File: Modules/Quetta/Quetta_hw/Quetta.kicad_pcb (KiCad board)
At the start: 2 copper layers, 89 parts, among them Q1 IRLML9303, SW1 SWITCH_H

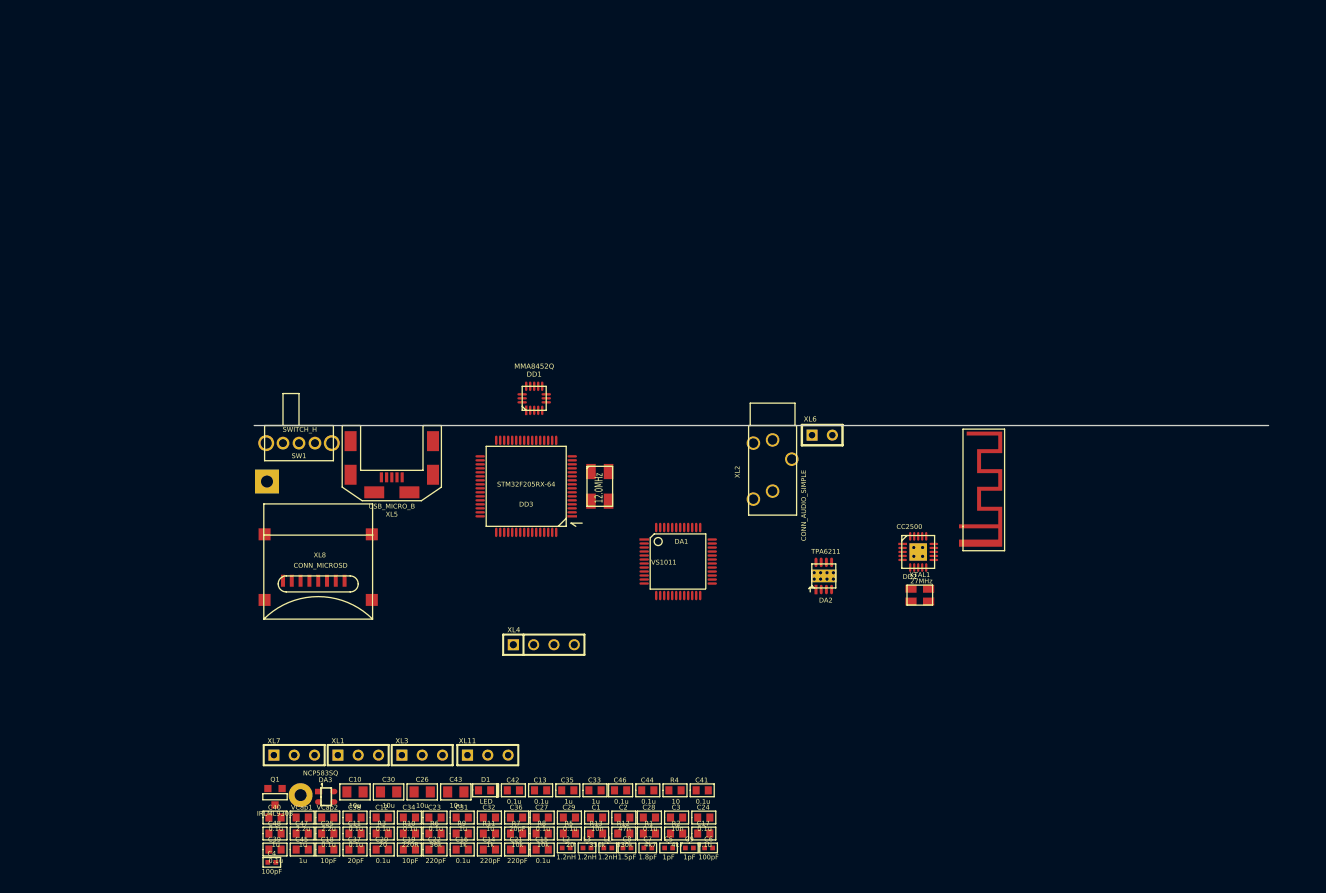
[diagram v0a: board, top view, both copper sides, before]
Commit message: 
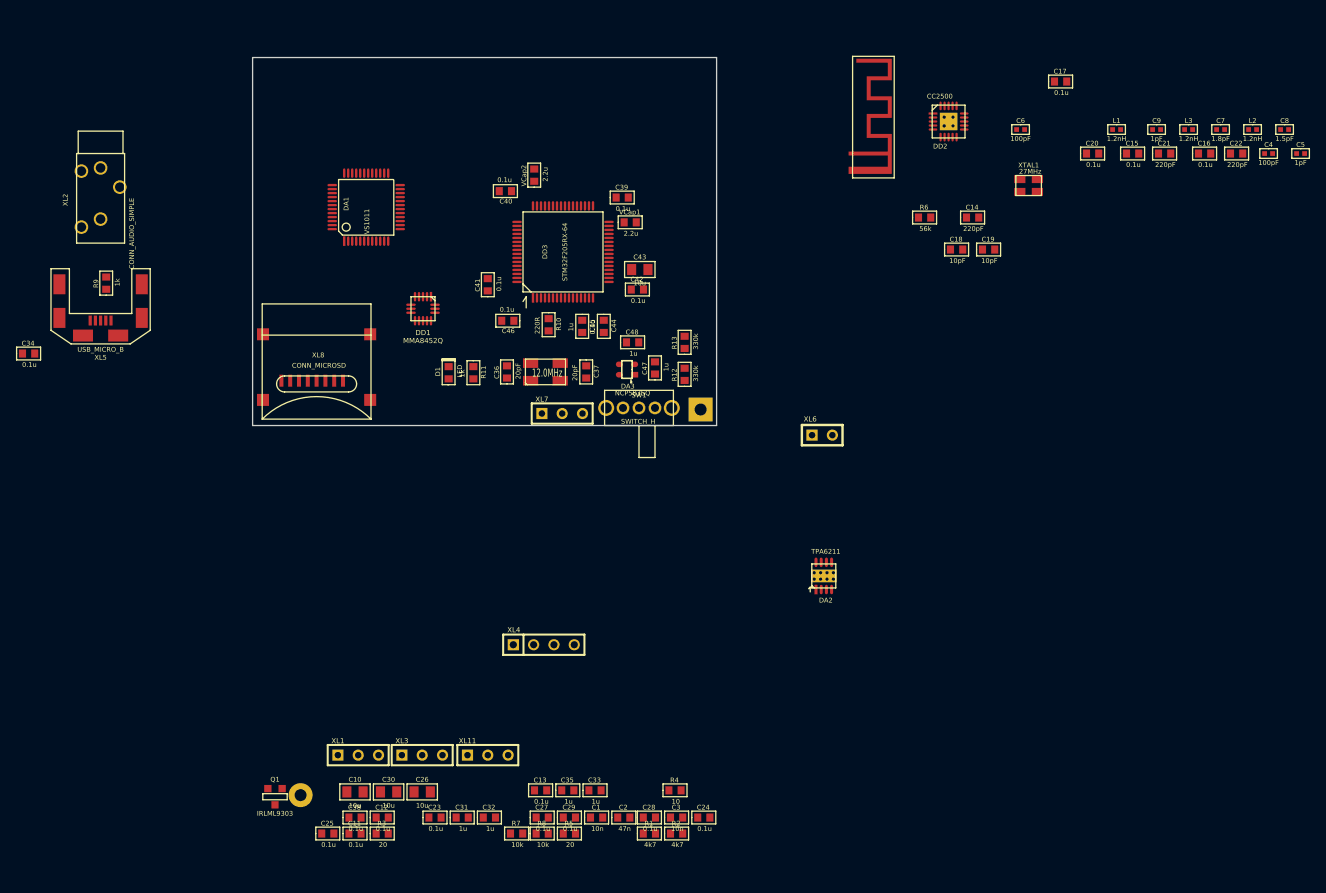
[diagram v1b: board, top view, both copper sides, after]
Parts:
- moved C4 152.9 mm to (287.0, 106.0)
- moved C22 132.7 mm to (283.0, 106.0)
- moved C16 127.2 mm to (279.0, 106.0)
- moved C20 124.3 mm to (265.0, 106.0)
- moved L2 124.2 mm to (285.0, 103.0)
- moved C8 121.7 mm to (289.0, 103.0)
- moved C21 118.9 mm to (274.0, 106.0)
- moved C5 117.4 mm to (291.0, 106.0)
- moved L3 117.1 mm to (277.0, 103.0)
- moved C7 114.9 mm to (281.0, 103.0)
- moved C15 114.1 mm to (270.0, 106.0)
- moved L1 110.0 mm to (268.0, 103.0)
- moved C18 108.6 mm to (248.0, 118.0)
- moved C9 107.1 mm to (273.0, 103.0)
- moved C19 104.2 mm to (252.0, 118.0)
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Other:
- board outline added: 58 x 46 mm

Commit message: 
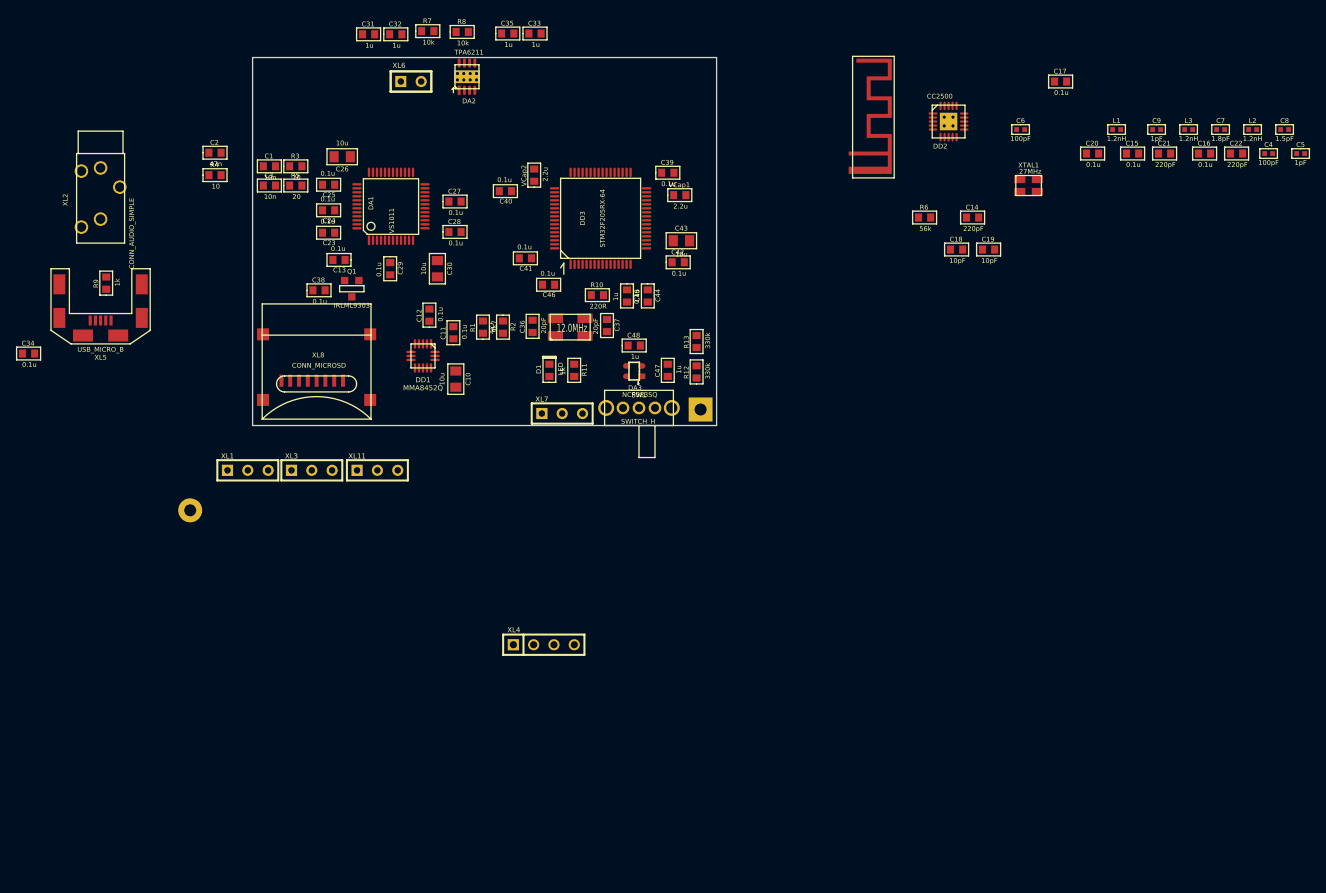
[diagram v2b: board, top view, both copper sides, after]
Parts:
- moved R7 100.9 mm to (181.9, 90.7)
- moved R8 100.7 mm to (186.2, 90.8)
- moved C31 98.6 mm to (174.5, 91.1)
- moved C32 98.6 mm to (177.9, 91.1)
- moved C2 97.6 mm to (155.3, 105.9)
- moved R4 96.0 mm to (155.3, 108.7)
- moved C33 94.9 mm to (195.3, 91.0)
- moved C35 94.9 mm to (191.9, 91.0)
- moved C3 94.0 mm to (162.1, 110.0)
- moved C1 91.1 mm to (162.1, 107.6)
- moved C24 89.2 mm to (169.5, 113.1), turned to 180 degrees
- moved R5 87.9 mm to (165.4, 110.0)
- moved R3 84.1 mm to (165.4, 107.6)
- moved C25 81.1 mm to (169.5, 109.9), turned to 180 degrees
- moved C26 80.0 mm to (171.2, 106.4), turned to 180 degrees
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
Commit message: quetta fsx added
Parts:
- moved XL10 78.5 mm to (216.0, 104.9)
- moved C8 71.0 mm to (223.9, 131.6), turned to 180 degrees
- moved C5 70.9 mm to (223.3, 127.2), turned to 270 degrees
- moved L2 66.2 mm to (224.4, 129.7), turned to 90 degrees
- moved C4 65.5 mm to (223.8, 123.0), turned to 270 degrees
- moved C7 63.9 mm to (222.7, 129.2), turned to 180 degrees
- moved XL4 63.1 mm to (192.9, 104.4)
- moved XL1 59.3 mm to (202.0, 104.4)
- moved L3 57.1 mm to (225.3, 127.2), turned to 90 degrees
- moved XL11 53.6 mm to (209.9, 104.4)
- moved C9 52.2 mm to (225.8, 125.3)
- moved L1 50.4 mm to (222.8, 125.3)
- moved C16 49.5 mm to (229.6, 106.5), turned to 90 degrees
- moved C21 49.1 mm to (225.2, 112.2), turned to 270 degrees
- moved C22 47.9 mm to (235.2, 109.5)
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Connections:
- ANT1 pad 1: N-0000038 -> GND
- C8 pad 1: N-0000038 -> GND
- L2 pad 1: N-0000038 -> GND
- SW1 pad 1: /BATTERY_PLUS -> (no net)
- SW1 pad 3: (no net) -> /BATTERY_PLUS
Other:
- net class Default: clearance 0.254 -> 0.2; trace_width 0.254 -> 0.2; via_dia 0.889 -> 0.9; via_drill 0.635 -> 0.4
- net class wide added: clearance 0.2, trace_width 0.5, via_dia 0.9, via_drill 0.4
- rule trace_clearance: 0.254 -> 0.2
- rule trace_min: 0.254 -> 0.2
- rule via_min_drill: 0.508 -> 0.4
- rule via_min_size: 0.889 -> 0.9

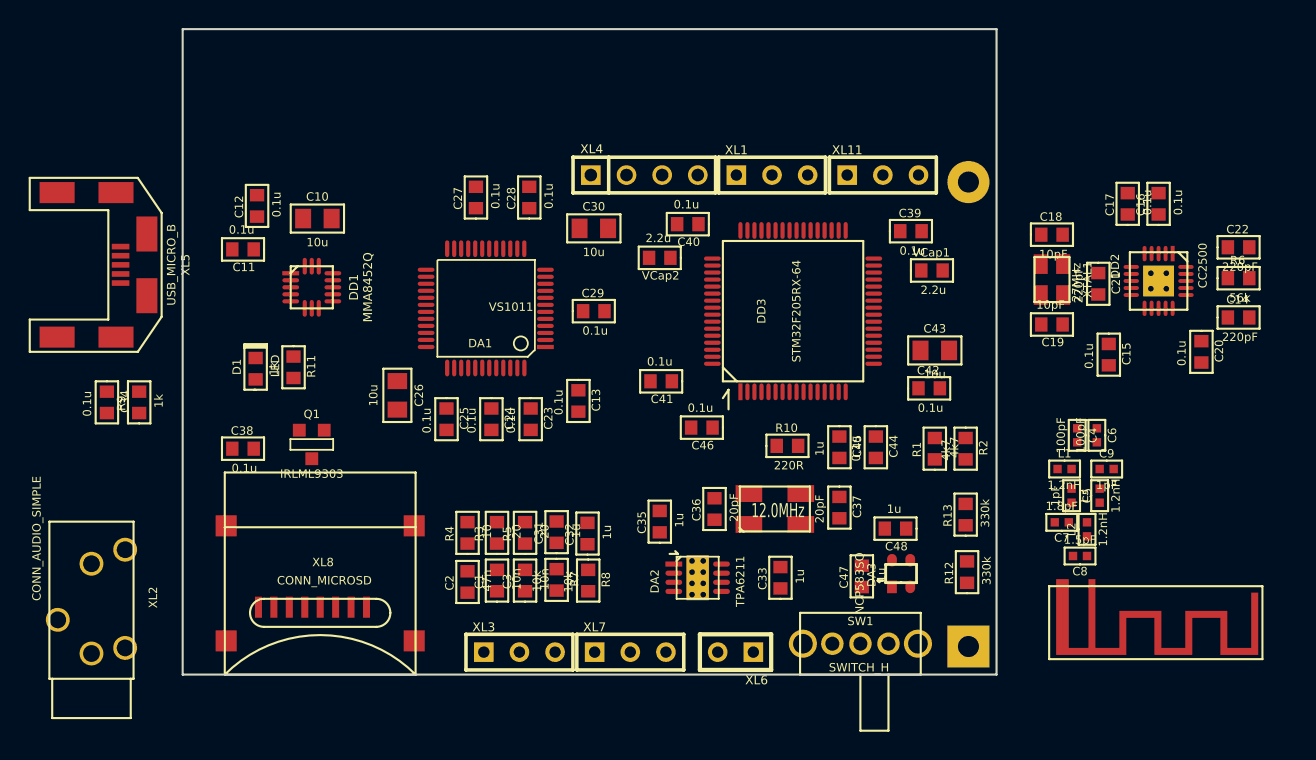
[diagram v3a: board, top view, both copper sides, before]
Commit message: 
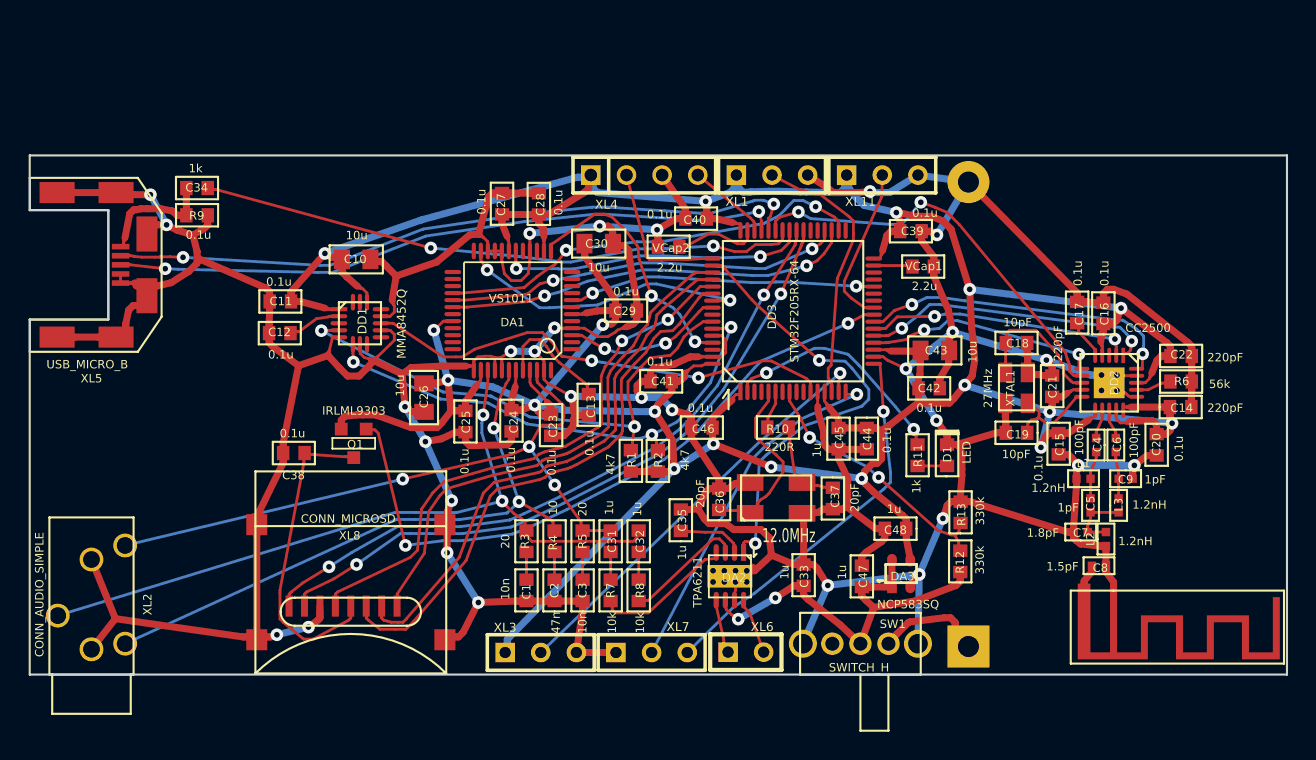
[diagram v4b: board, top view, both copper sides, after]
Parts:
- moved D1 49.7 mm to (214.5, 124.4)
- moved R11 44.9 mm to (212.4, 124.4)
- moved R2 22.0 mm to (193.9, 124.8)
- moved R1 21.7 mm to (191.9, 124.8)
- moved R9 15.8 mm to (161.0, 105.3), turned to 180 degrees
- moved C34 14.8 mm to (161.0, 107.3), turned to 0 degrees
- moved C12 9.21 mm to (166.9, 115.7), turned to 180 degrees
- moved C22 8.76 mm to (231.2, 117.3)
- moved C16 8.74 mm to (225.6, 114.3)
- moved C17 8.55 mm to (223.7, 114.2)
- moved R6 8.43 mm to (231.2, 119.1)
- moved C19 8.12 mm to (219.4, 122.8)
- moved XTAL1 8.12 mm to (219.4, 119.6)
- moved C18 8.12 mm to (219.4, 116.4)
- moved DD2 8.06 mm to (226.0, 119.2)
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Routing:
- net GND: track 0.00 -> 467.4 mm, vias 0 -> 29
- net +3.3V: track 0.00 -> 318.4 mm, vias 0 -> 18
- net /SND_R: track 0.00 -> 54.3 mm, vias 0 -> 2
- net /USB_DM: track 0.00 -> 49.3 mm, vias 0 -> 2
- net /SD_DAT1: track 0.00 -> 48.4 mm, vias 0 -> 2
- net /SD_DAT0: track 0.00 -> 48.0 mm, vias 0 -> 2
- net /USB_DP: track 0.00 -> 47.5 mm, vias 0 -> 2
- net /SD_POWER: track 0.00 -> 47.5 mm, vias 0 -> 2
- net /SND_L: track 0.00 -> 46.8 mm, vias 0 -> 3
- net /SND_C: track 0.00 -> 43.7 mm, vias 0 -> 2
- net N-0000062: track 0.00 -> 42.7 mm, vias 0 -> 2
- net /SD_CMD: track 0.00 -> 39.3 mm
- net /SD_CLK: track 0.00 -> 39.3 mm, vias 0 -> 2
- net /SD_DAT3: track 0.00 -> 38.3 mm
- net /I2C_SCL: track 0.00 -> 37.8 mm, vias 0 -> 2
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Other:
- board size 58 x 46 mm -> 89.6 x 37 mm

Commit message: + Quetta Gerber + Quetta Portrait, speaking
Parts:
- removed C2: 47n, CAP_0603
- removed C4, C6: 100pF, CAP_0402
- removed C5, C9: 1pF, CAP_0402
- removed C7: 1.8pF, CAP_0402
- removed C8: 1.5pF, CAP_0402
- removed L1, L2, L3: 1.2nH, IND_0402
- removed XL2: CONN_AUDIO_SIMPLE, CONN_AUDIO_CKX3_5_30
- added HOLE1: HOLE_METALLED, Hole3_5_out6mm, F.Cu at (187.4, 104.4)
- added HOLE2: HOLE_METALLED, Hole3_5_out6mm, F.Cu at (187.4, 140.0)
- added HOLE3: HOLE_METALLED, Hole3_5_out6mm, F.Cu at (224.2, 104.4)
- added HOLE4: HOLE_METALLED, Hole3_5_out6mm, F.Cu at (224.2, 140.0)
- added Q2: BC817, SOT23, F.Cu at (218.2, 133.0)
- ANT1: value ANT_GENERAL -> ANT_PCB_NOCNTR; footprint ANT_2400_MEANDER -> ANT_FOLDED_DIPOLE2
- R12, R13: value 330k -> 100k
- R4: value 10 -> 1k
- moved C38 51.5 mm to (219.0, 117.8), turned to 270 degrees
- moved XL8 48.2 mm to (213.6, 108.4), turned to 90 degrees
- moved XL3 45.9 mm to (222.6, 111.4), turned to 270 degrees
- moved Q1 44.8 mm to (216.6, 117.8), turned to 90 degrees
- moved XL5 42.1 mm to (196.6, 106.6), turned to 270 degrees
- moved C34 39.5 mm to (199.8, 114.6), turned to 90 degrees
- moved XL10 39.0 mm to (202.2, 141.4)
- moved R9 38.3 mm to (198.2, 114.6), turned to 270 degrees
- moved C11 37.6 mm to (196.4, 136.8), turned to 270 degrees
- moved C12 37.6 mm to (198.0, 136.8), turned to 270 degrees
- moved R4 31.7 mm to (218.2, 130.2), turned to 0 degrees
- moved DD1 30.5 mm to (197.8, 132.2), turned to 0 degrees
- moved C10 29.6 mm to (196.6, 127.4), turned to 90 degrees
- moved XL7 27.3 mm to (188.2, 111.6), turned to 270 degrees
- moved D1 25.6 mm to (191.8, 112.4), turned to 180 degrees
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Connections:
- ANT1 pad 1: GND -> /Ant1
- ANT1 pad 2: GND -> /Ant2
- C22 pad 1: +3.3V -> N-0000023
- DA1 pad 42: /SND_C -> (no net)
- DD2 pad 18: +3.3V -> N-0000023
- DD3 pad 9: (no net) -> /BAT_MEASURE
- R13 pad 2: GND -> N-0000045
- R4 pad 1: N-0000046 -> /BAT_MEASURE
- R4 pad 2: /SND_C -> N-0000046
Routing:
- net +3.3V: track 318.4 -> 244.8 mm, vias 18 -> 20
- net /SND_C: track 43.7 -> 0.00 mm, vias 2 -> 0
- net /SD_POWER: track 47.5 -> 9.32 mm, vias 2 -> 0
- net /SND_R: track 54.3 -> 17.2 mm
- net GND: track 467.4 -> 502.0 mm, vias 29 -> 83
- net /SD_DAT0: track 48.0 -> 14.4 mm
- net /USB_DM: track 49.3 -> 16.1 mm, vias 2 -> 0
- net /SD_DAT1: track 48.4 -> 15.5 mm
- net /USB_DP: track 47.5 -> 16.1 mm, vias 2 -> 0
- net N-0000055: track 42.7 -> 12.3 mm, vias 2 -> 0
- net /SND_L: track 46.8 -> 20.8 mm, vias 3 -> 2
- net /I2C_SDA: track 36.0 -> 12.4 mm, vias 3 -> 0
- net /I2C_SCL: track 37.8 -> 16.2 mm
- net /SD_DAT3: track 38.3 -> 18.0 mm, vias 0 -> 2
- net /ACC_IRQ: track 33.9 -> 14.1 mm
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- added copper zone on B.Cu, net GND
- added copper zone on F.Cu, net GND
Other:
- board size 89.6 x 37 mm -> 87.5 x 42.4 mm
- rule pad_to_mask_clearance: 0.2 -> 0.075
